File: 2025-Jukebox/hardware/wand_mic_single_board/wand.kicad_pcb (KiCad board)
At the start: 4 copper layers, 17.5 x 63 mm, 52 parts, among them J1 USB_C_Receptacle_USB2.0, J4 Conn_01x02, J9 Conn_01x02, Q1 MUN5214DW1T1G, Q3 CJ3139K, SW1 SW_Push, U1 CP2104, U2 ESP32-PICO-D4, U3 ICM-20948, U4 TP4065-4.2V, U5 TLV76718DRVx, U6 LY68L6400SLIT, U7 PCA9306, U9 TLV76733DRVx

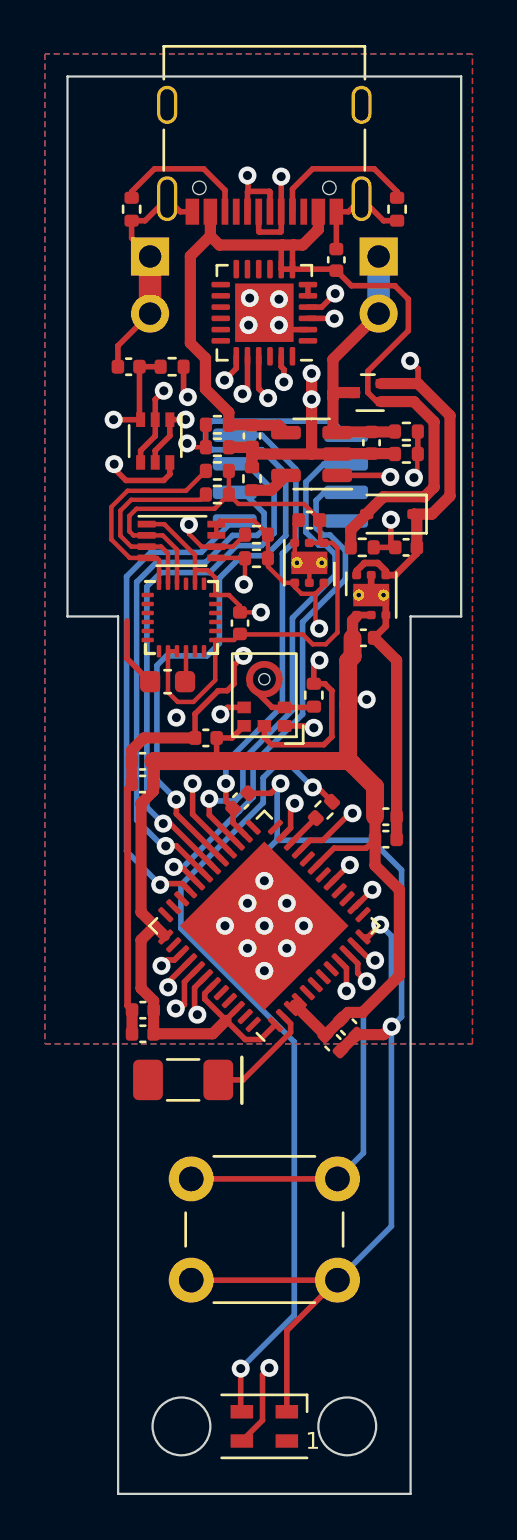
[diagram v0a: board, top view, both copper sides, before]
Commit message: Replaced IMU with BNO055
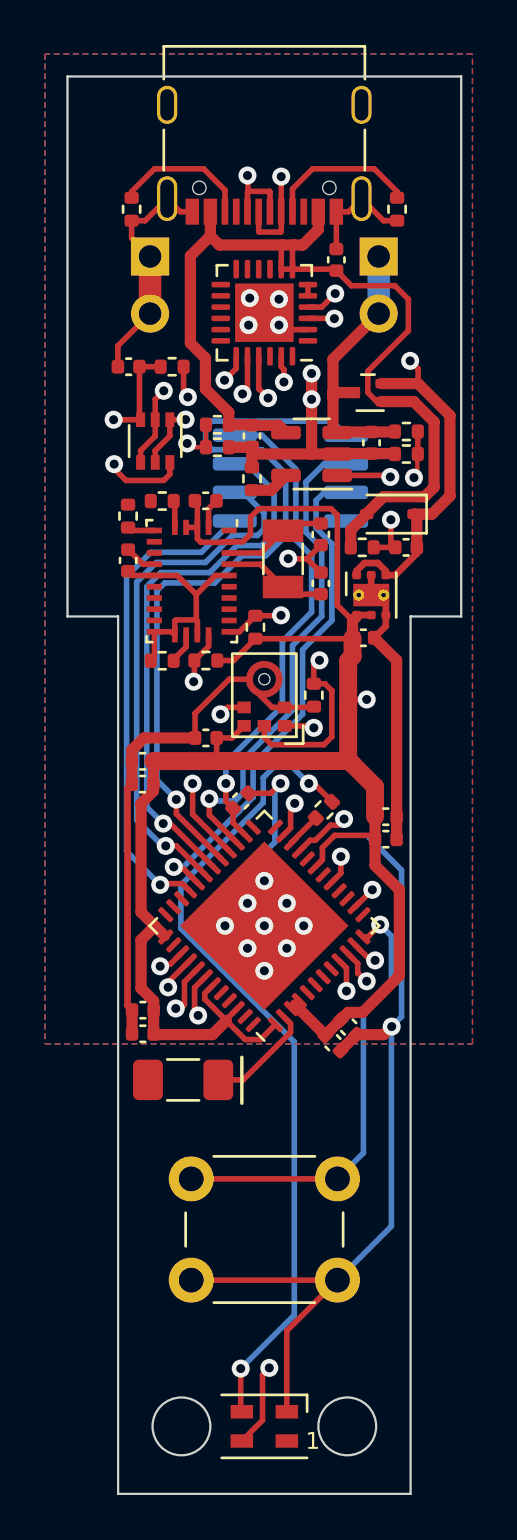
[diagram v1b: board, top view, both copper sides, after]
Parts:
- removed R10, R9: 2.2k, Resistor_SMD:R_0402_1005Metric
- removed U3: ICM-20948, Sensor_Motion:InvenSense_QFN-24_3x3mm_P0.4mm
- removed U5: TLV76718DRVx, Package_SON:WSON-6-1EP_2x2mm_P0.65mm_EP1x1.6mm_ThermalVias
- removed U7: PCA9306, Package_SO:VSSOP-8_2.3x2mm_P0.5mm
- added C14: 22p, Capacitor_SMD:C_0402_1005Metric, F.Cu at (145.2, 87.5)
- added R1: 10k, Resistor_SMD:R_0402_1005Metric, F.Cu at (138.1, 93.2)
- added R15: 10k, Resistor_SMD:R_0402_1005Metric, F.Cu at (142.2, 91.7)
- added R16: 10k, Resistor_SMD:R_0402_1005Metric, F.Cu at (140.0, 93.1)
- added U8: BNO055, Package_LGA:LGA-28_5.2x3.8mm_P0.5mm, F.Cu at (139.4, 89.6)
- added Y1: 32.768kHz, Crystal:Crystal_SMD_3215-2Pin_3.2x1.5mm, F.Cu at (143.5, 88.6)
- C12: value 10u -> 100n
- C13: value 100n -> 22p
- C9: footprint Capacitor_SMD:C_0603_1608Metric -> Capacitor_SMD:C_0402_1005Metric
- R13, R14: value 2.2k -> 10k
- moved C12 8.25 mm to (136.6, 88.7), turned to -90 degrees
- moved C9 8.22 mm to (140.0, 86.0), turned to 0 degrees
- moved R13 4.08 mm to (136.6, 86.7), turned to -90 degrees
- moved C13 4.00 mm to (145.2, 89.7)
- moved R14 2.79 mm to (138.1, 86.1), turned to 0 degrees
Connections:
- C12 pad 1: +1V8 -> Net-(U8-CAP)
- C13 pad 1: +1V8 -> Net-(U8-XOUT32)
- C9 pad 1: Net-(U3-REGOUT) -> +3V3
- R13 pad 1: +1V8 -> GND
- R13 pad 2: IMU_SCL_1V8 -> Net-(U8-PS0)
- R14 pad 1: +1V8 -> GND
- R14 pad 2: IMU_SDA_1V8 -> Net-(U8-PS1)
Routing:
- net +1V8: track 33.9 -> 0.00 mm
- net GND: track 176.8 -> 151.1 mm, vias 21 -> 19
- net IMU_SDA_1V8: track 9.86 -> 0.00 mm
- net +3V3: track 93.0 -> 102.5 mm, vias 3 -> 2
- net IMU_SCL_1V8: track 9.01 -> 0.00 mm
- net IMU_SCL: track 27.6 -> 32.9 mm
- net Net-(U8-XOUT32): track 0.00 -> 4.63 mm
- net Net-(U8-XIN32): track 0.00 -> 4.62 mm
- net IMU_SDA: track 26.3 -> 29.8 mm
- net Net-(U8-CAP): track 0.00 -> 1.44 mm
- net Net-(U8-COM3): track 0.00 -> 1.38 mm
- net Net-(U3-REGOUT): track 1.37 -> 0.00 mm
- net Net-(U8-PS0): track 0.00 -> 1.22 mm
- net Net-(U8-PS1): track 0.00 -> 1.19 mm
- net GPIO14: track 13.1 -> 12.4 mm
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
